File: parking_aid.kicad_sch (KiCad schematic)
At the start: 29 parts, among them U1 LM555xN, U2 LM324A, U3 LM324A

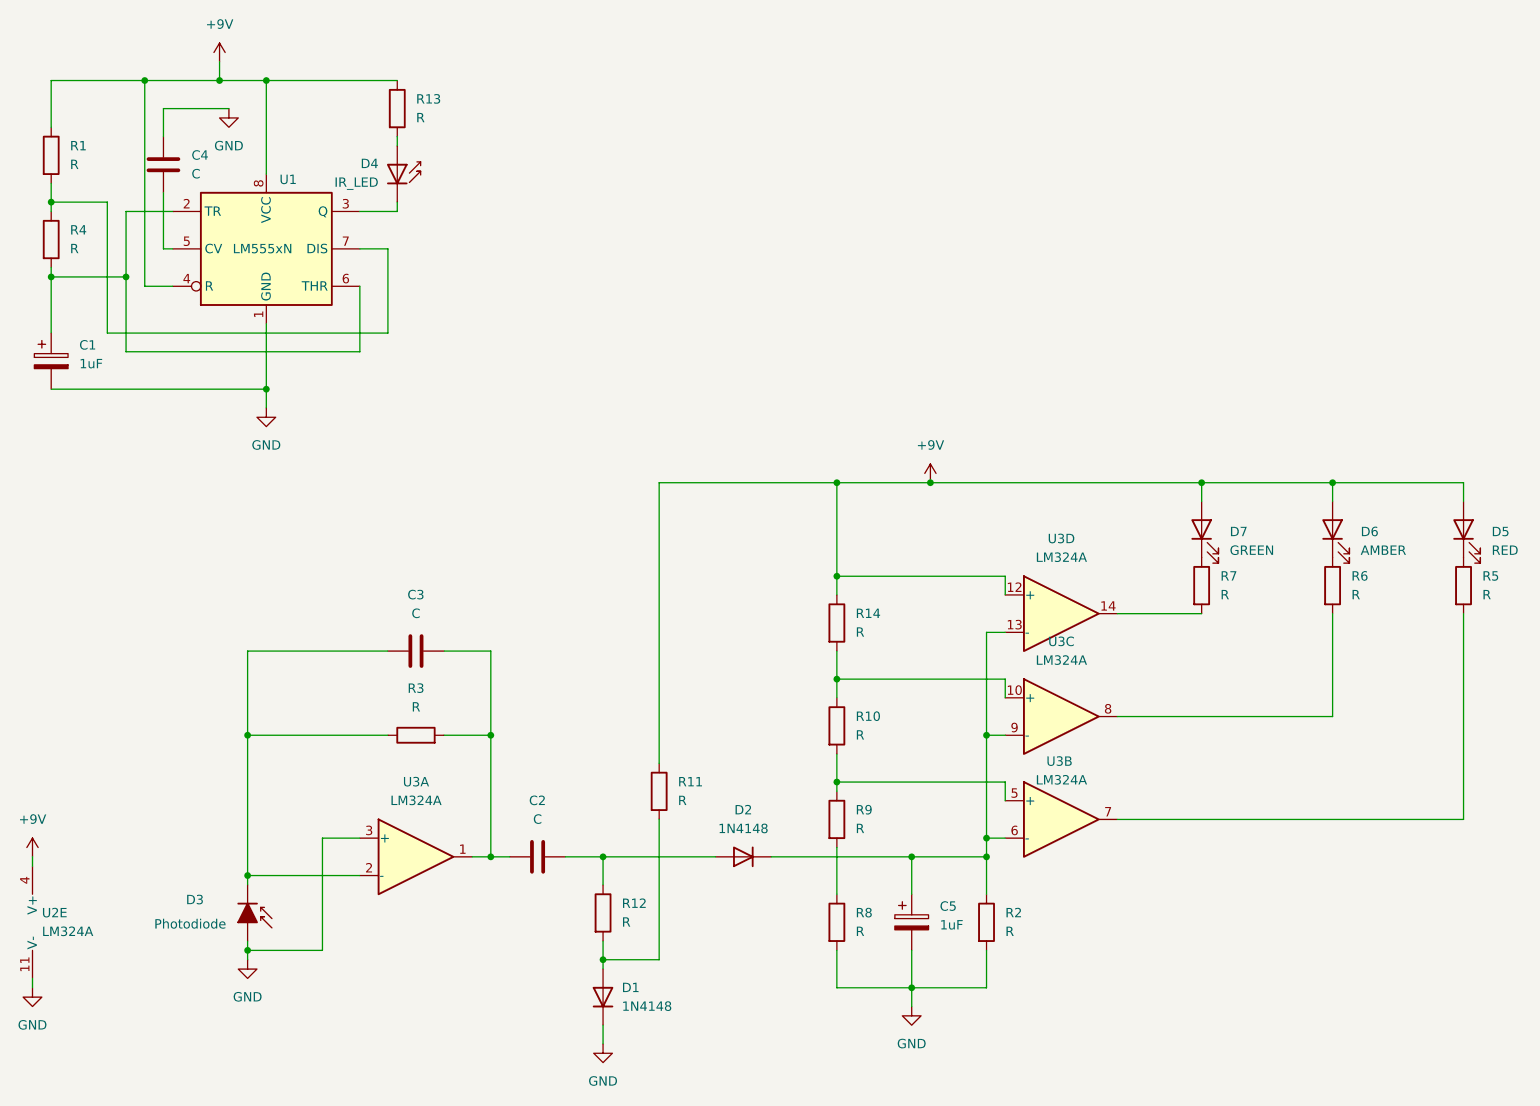
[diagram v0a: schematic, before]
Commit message: added values for all components
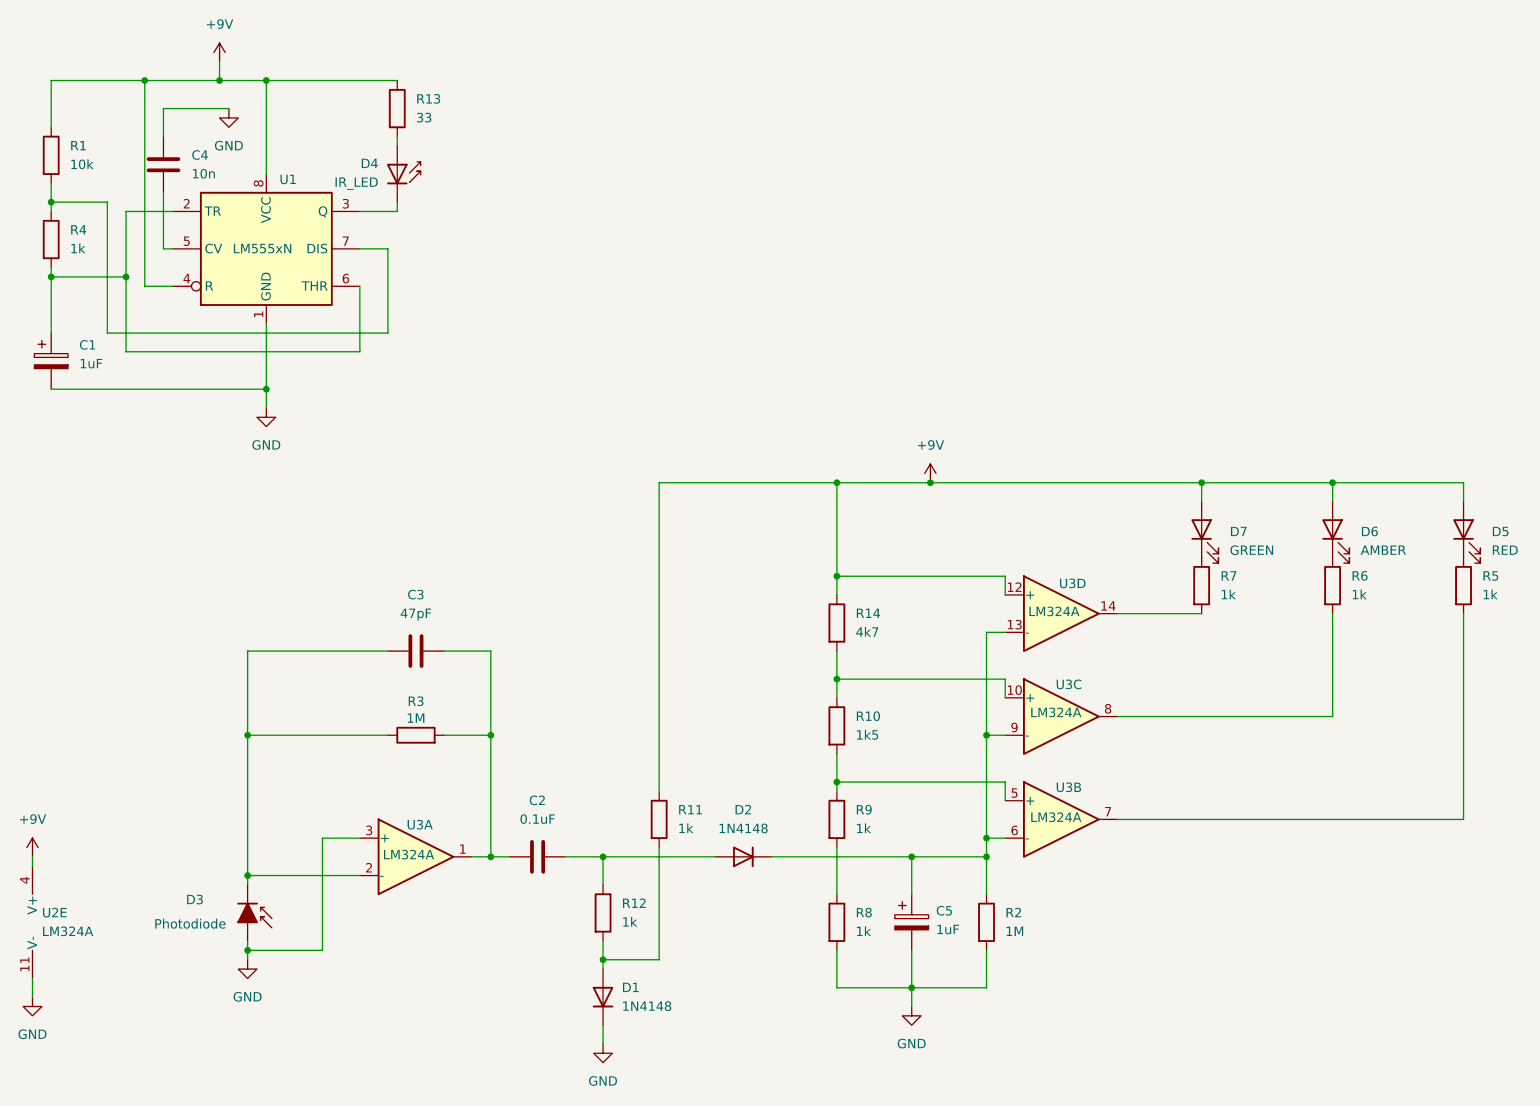
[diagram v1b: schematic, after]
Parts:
- C2: value C -> 0.1uF
- C3: value C -> 47pF
- C4: value C -> 10n
- R1: value R -> 10k
- R10: value R -> 1k5
- R11, R12, R4, R5, R6, R7, R8, R9: value R -> 1k
- R13: value R -> 33
- R14: value R -> 4k7
- R2, R3: value R -> 1M
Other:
- company: University of Derby -> (none)
- title: Pakring Aid -> (none)
- moved on the sheet: R11
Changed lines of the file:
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@@
 	(generator_version "8.0")
 	(paper "A4")
-	(title_block
-		(title "Pakring Aid")
-		(date "2017-07-31")
-		(rev "2")
-		(company "University of Derby")
-		(comment 1 "David WIlson")
-	)
 	(junction
 		(at 172.72 123.19)
@@
 	(wire
 		(pts
-			(xy 43.18 156.21) (xy 43.18 157.48)
+			(xy 43.18 156.21) (xy 43.18 158.75)
 		)
 		(stroke
@@
 	(wire
 		(pts
-			(xy 128.27 127) (xy 128.27 88.9)
+			(xy 128.27 130.81) (xy 128.27 88.9)
 		)
 		(stroke
@@
 	(wire
 		(pts
-			(xy 128.27 153.67) (xy 128.27 134.62)
+			(xy 128.27 153.67) (xy 128.27 138.43)
 		)
 		(stroke
@@
 			)
 		)
-		(property "Value" "C"
+		(property "Value" "0.1uF"
 			(at 111.76 134.62 90)
 			(effects
@@
 			)
 		)
-		(property "Value" "R"
+		(property "Value" "1k"
 			(at 123.19 148.5899 0)
 			(effects
@@
 		(dnp no)
 		(property "Reference" "U3"
-			(at 182.626 126.746 0)
+			(at 183.896 130.302 0)
 			(effects
 				(font
@@
 		)
 		(property "Value" "LM324A"
-			(at 182.88 129.286 0)
+			(at 182.118 134.366 0)
 			(effects
 				(font
@@
 			)
 		)
-		(property "Value" "R"
+		(property "Value" "1M"
 			(at 175.26 149.8599 0)
 			(effects
@@
 	(symbol
 		(lib_id "Device:R")
-		(at 128.27 130.81 0)
+		(at 128.27 134.62 0)
 		(unit 1)
 		(exclude_from_sim no)
@@
 		(fields_autoplaced yes)
 		(property "Reference" "R11"
-			(at 130.81 129.5399 0)
+			(at 130.81 133.3499 0)
 			(effects
 				(font
@@
 			)
 		)
-		(property "Value" "R"
-			(at 130.81 132.0799 0)
+		(property "Value" "1k"
+			(at 130.81 135.8899 0)
 			(effects
 				(font
@@
 		)
 		(property "Footprint" "Resistor_THT:R_Axial_DIN0207_L6.3mm_D2.5mm_P7.62mm_Horizontal"
-			(at 126.492 130.81 90)
+			(at 126.492 134.62 90)
 			(effects
 				(font
@@
 		)
 		(property "Datasheet" "~"
-			(at 128.27 130.81 0)
+			(at 128.27 134.62 0)
 			(effects
 				(font
@@
 		)
 		(property "Description" "Resistor"
-			(at 128.27 130.81 0)
+			(at 128.27 134.62 0)
 			(effects
 				(font
@@
 	(symbol
 		(lib_id "power:GND")
-		(at 43.18 157.48 0)
+		(at 43.18 158.75 0)
 		(unit 1)
 		(exclude_from_sim no)
@@
 		(fields_autoplaced yes)
 		(property "Reference" "#PWR07"
-			(at 43.18 163.83 0)
+			(at 43.18 165.1 0)
 			(effects
 				(font
@@
 		)
 		(property "Value" "GND"
-			(at 43.18 162.56 0)
+			(at 43.18 163.83 0)
 			(effects
 				(font
@@
 		)
 		(property "Footprint" ""
-			(at 43.18 157.48 0)
+			(at 43.18 158.75 0)
 			(effects
 				(font
@@
 		)
 		(property "Datasheet" ""
-			(at 43.18 157.48 0)
+			(at 43.18 158.75 0)
 			(effects
 				(font
@@
 		)
 		(property "Description" "Power symbol creates a global label with name \"GND\" , ground"
-			(at 43.18 157.48 0)
+			(at 43.18 158.75 0)
 			(effects
 				(font
@@
 			)
 		)
-		(property "Value" "R"
+		(property "Value" "1k"
 			(at 222.25 104.1399 0)
 			(effects
@@
 		(on_board yes)
 		(dnp no)
-		(fields_autoplaced yes)
 		(property "Reference" "R3"
-			(at 95.25 116.84 90)
+			(at 95.25 118.618 90)
 			(effects
 				(font
@@
 			)
 		)
-		(property "Value" "R"
-			(at 95.25 119.38 90)
+		(property "Value" "1M"
+			(at 95.25 120.904 90)
 			(effects
 				(font
@@
 		(on_board yes)
 		(dnp no)
-		(fields_autoplaced yes)
 		(property "Reference" "C5"
-			(at 166.37 146.4309 0)
+			(at 165.862 147.066 0)
 			(effects
 				(font
@@
 		)
 		(property "Value" "1uF"
-			(at 166.37 148.9709 0)
+			(at 165.862 149.606 0)
 			(effects
 				(font
@@
 			)
 		)
-		(property "Value" "R"
+		(property "Value" "10k"
 			(at 48.26 45.7199 0)
 			(effects
@@
 			)
 		)
-		(property "Value" "R"
+		(property "Value" "1k"
 			(at 154.94 135.8899 0)
 			(effects
@@
 			)
 		)
-		(property "Value" "R"
+		(property "Value" "33"
 			(at 95.25 39.3699 0)
 			(effects
@@
 			)
 		)
-		(property "Value" "C"
+		(property "Value" "47pF"
 			(at 95.25 106.68 90)
 			(effects
@@
 			)
 		)
-		(property "Value" "R"
+		(property "Value" "1k"
 			(at 204.47 104.1399 0)
 			(effects
@@
 		(on_board yes)
 		(dnp no)
-		(fields_autoplaced yes)
 		(property "Reference" "U3"
-			(at 95.25 129.54 0)
+			(at 95.758 135.382 0)
 			(effects
 				(font
@@
 		)
 		(property "Value" "LM324A"
-			(at 95.25 132.08 0)
+			(at 94.234 139.446 0)
 			(effects
 				(font
@@
 			)
 		)
-		(property "Value" "R"
+		(property "Value" "1k"
 			(at 240.03 104.1399 0)
 			(effects
@@
 		(on_board yes)
 		(dnp no)
-		(fields_autoplaced yes)
 		(property "Reference" "U3"
-			(at 182.88 110.49 0)
+			(at 183.896 116.332 0)
 			(effects
 				(font
@@
 		)
 		(property "Value" "LM324A"
-			(at 182.88 113.03 0)
+			(at 182.118 120.142 0)
 			(effects
 				(font
@@
 			)
 		)
-		(property "Value" "C"
+		(property "Value" "10n"
 			(at 64.77 46.9899 0)
 			(effects
@@
 			)
 		)
-		(property "Value" "R"
+		(property "Value" "1k"
 			(at 154.94 149.8599 0)
 			(effects
@@
 			)
 		)
-		(property "Value" "R"
+		(property "Value" "4k7"
 			(at 154.94 109.2199 0)
 			(effects
@@
 			)
 		)
-		(property "Value" "R"
+		(property "Value" "1k5"
 			(at 154.94 123.1899 0)
 			(effects
@@
 			)
 		)
-		(property "Value" "R"
+		(property "Value" "1k"
 			(at 48.26 57.1499 0)
 			(effects
@@
 		(on_board yes)
 		(dnp no)
-		(fields_autoplaced yes)
 		(property "Reference" "U3"
-			(at 182.88 96.52 0)
+			(at 184.404 102.616 0)
 			(effects
 				(font
@@
 		)
 		(property "Value" "LM324A"
-			(at 182.88 99.06 0)
+			(at 181.864 106.426 0)
 			(effects
 				(font
